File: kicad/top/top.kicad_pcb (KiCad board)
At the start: 2 copper layers, 62 x 119.5 mm, 32 parts, among them J1 OLED_128x64, J2 Conn_01x15, SW1 SW_SPDT, SW2 RotaryEncoder_Switch

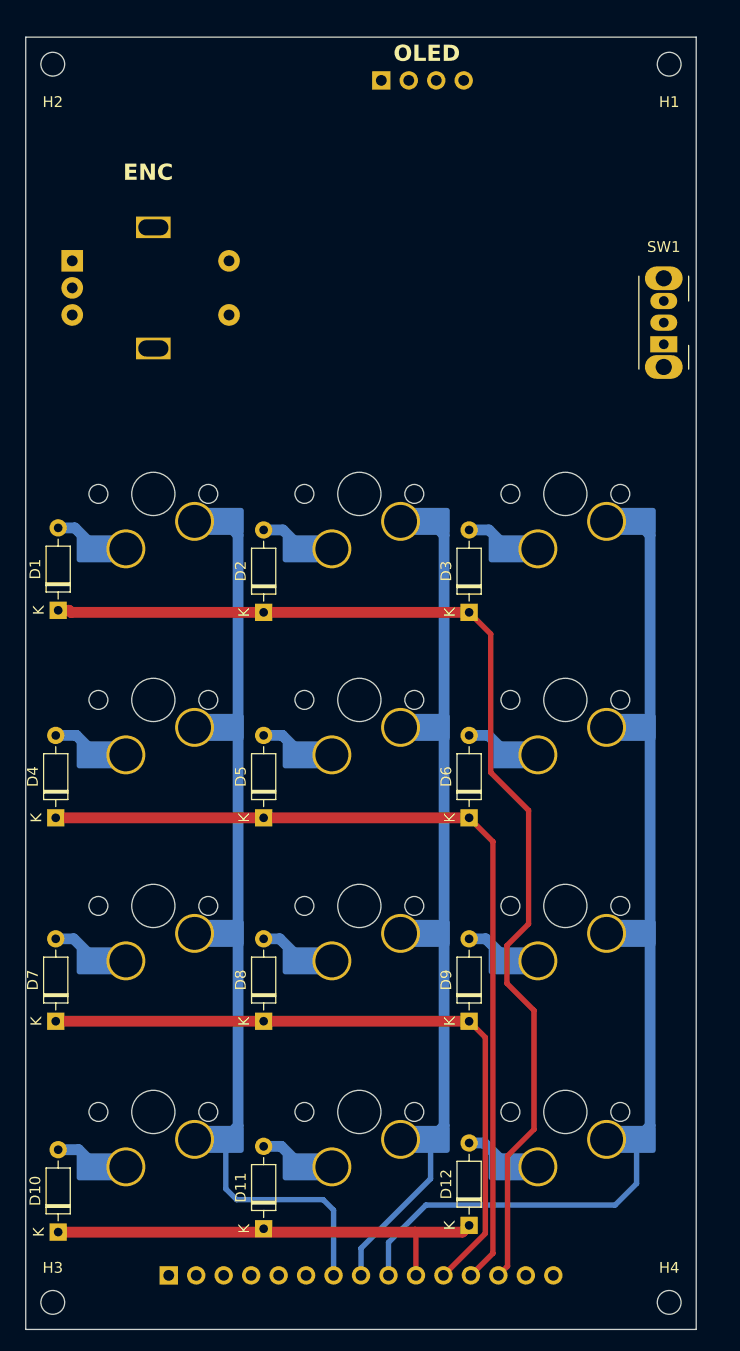
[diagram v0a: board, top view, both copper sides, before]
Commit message: added bottom part of pcb, added 3d model for adafruit feather v2
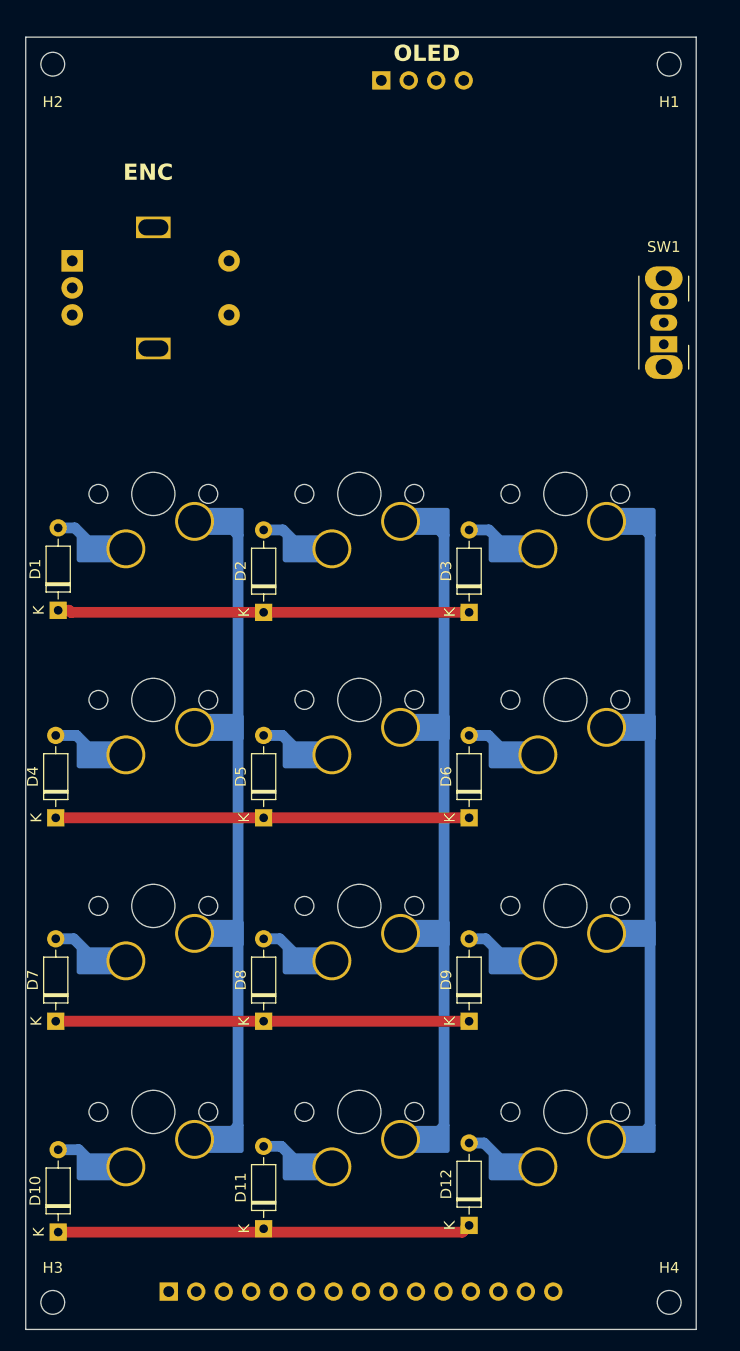
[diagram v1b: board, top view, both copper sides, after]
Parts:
- moved J2 1.50 mm to (27.3, 135.9)
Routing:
- net ROW0: track 104.9 -> 38.1 mm
- net ROW1: track 82.3 -> 38.2 mm
- net COL2: track 90.5 -> 58.2 mm
- net ROW2: track 64.0 -> 38.2 mm
- net COL0: track 79.5 -> 58.2 mm
- net COL1: track 73.4 -> 58.2 mm
- net ROW3: track 42.3 -> 38.3 mm
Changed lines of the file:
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@@
 	(footprint "Connector_PinHeader_2.54mm:PinHeader_1x15_P2.54mm_Vertical"
 		(layer "B.Cu")
-		(at 27.2725 134.425 -90)
+		(at 27.2725 135.925 -90)
 		(descr "Through hole straight pin header, 1x15, 2.54mm pitch, single row")
 		(tags "Through hole pin header THT 1x15 2.54mm single row")
@@
 	)
 	(segment
-		(start 61.0475 120.925)
-		(end 61.0475 109.925)
-		(width 0.5)
-		(layer "F.Cu")
-		(net 1)
-	)
-	(segment
-		(start 58.6025 123.37)
-		(end 61.0475 120.925)
-		(width 0.5)
-		(layer "F.Cu")
-		(net 1)
-	)
-	(segment
-		(start 58.5475 107.425)
-		(end 58.5475 103.925)
-		(width 0.5)
-		(layer "F.Cu")
-		(net 1)
-	)
-	(segment
-		(start 57.0475 87.925)
-		(end 57.0475 75.115)
-		(width 0.5)
-		(layer "F.Cu")
-		(net 1)
-	)
-	(segment
 		(start 18.0475 72.925)
 		(end 18.2375 73.115)
@@
 	)
 	(segment
-		(start 60.5475 91.425)
-		(end 57.0475 87.925)
-		(width 0.5)
-		(layer "F.Cu")
-		(net 1)
-	)
-	(segment
-		(start 60.5475 101.925)
-		(end 60.5475 91.425)
-		(width 0.5)
-		(layer "F.Cu")
-		(net 1)
-	)
-	(segment
 		(start 18.2375 73.115)
 		(end 55.0475 73.115)
@@
 	)
 	(segment
-		(start 57.0475 75.115)
-		(end 55.0475 73.115)
-		(width 0.5)
-		(layer "F.Cu")
-		(net 1)
-	)
-	(segment
-		(start 58.6025 133.575)
-		(end 58.6025 123.37)
-		(width 0.5)
-		(layer "F.Cu")
-		(net 1)
-	)
-	(segment
-		(start 57.7525 134.425)
-		(end 58.6025 133.575)
-		(width 0.5)
-		(layer "F.Cu")
-		(net 1)
-	)
-	(segment
 		(start 17.0475 72.925)
 		(end 18.0475 72.925)
@@
 	)
 	(segment
-		(start 61.0475 109.925)
-		(end 58.5475 107.425)
-		(width 0.5)
-		(layer "F.Cu")
-		(net 1)
-	)
-	(segment
-		(start 58.5475 103.925)
-		(end 60.5475 101.925)
-		(width 0.5)
-		(layer "F.Cu")
-		(net 1)
-	)
-	(segment
 		(start 18.59 65.305)
 		(end 20.5275 67.2425)
@@
 	)
 	(segment
-		(start 55.2125 134.425)
-		(end 57.2475 132.39)
-		(width 0.5)
-		(layer "F.Cu")
-		(net 6)
-	)
-	(segment
 		(start 16.8225 92.115)
 		(end 55.0475 92.115)
@@
 	)
 	(segment
-		(start 57.2475 94.315)
-		(end 55.0475 92.115)
-		(width 0.5)
-		(layer "F.Cu")
-		(net 6)
-	)
-	(segment
-		(start 57.2475 132.39)
-		(end 57.2475 94.315)
-		(width 0.5)
-		(layer "F.Cu")
-		(net 6)
-	)
-	(segment
 		(start 56.83 84.495)
 		(end 58.6275 86.2925)
@@
 	)
 	(segment
-		(start 56.5475 112.425)
-		(end 55.0475 110.925)
-		(width 0.5)
-		(layer "F.Cu")
-		(net 9)
-	)
-	(segment
-		(start 56.5475 130.55)
-		(end 56.5475 112.425)
-		(width 0.5)
-		(layer "F.Cu")
-		(net 9)
-	)
-	(segment
 		(start 16.8225 110.925)
 		(end 55.0475 110.925)
@@
 	)
 	(segment
-		(start 52.6725 134.425)
-		(end 56.5475 130.55)
-		(width 0.5)
-		(layer "F.Cu")
-		(net 9)
-	)
-	(segment
 		(start 55.0475 103.305)
 		(end 56.59 103.305)
@@
 	)
 	(segment
-		(start 50.1325 134.425)
-		(end 50.1325 130.51)
-		(width 0.5)
-		(layer "F.Cu")
-		(net 13)
-	)
-	(segment
-		(start 50.1325 130.51)
-		(end 50.0475 130.425)
-		(width 0.5)
-		(layer "F.Cu")
-		(net 13)
-	)
-	(segment
 		(start 54.4275 130.425)
 		(end 55.0475 129.805)
@@
 	)
 	(segment
-		(start 50.0475 130.425)
-		(end 54.4275 130.425)
-		(width 1)
-		(layer "F.Cu")
-		(net 13)
-	)
-	(segment
 		(start 17.0475 130.425)
-		(end 50.0475 130.425)
+		(end 54.4275 130.425)
 		(width 1)
 		(layer "F.Cu")
@@
 	)
 	(segment
-		(start 41.5475 127.425)
-		(end 33.5475 127.425)
-		(width 0.5)
-		(layer "B.Cu")
-		(net 17)
-	)
-	(segment
-		(start 42.5125 128.39)
-		(end 41.5475 127.425)
-		(width 0.5)
-		(layer "B.Cu")
-		(net 17)
-	)
-	(segment
-		(start 42.5125 134.425)
-		(end 42.5125 128.39)
-		(width 0.5)
-		(layer "B.Cu")
-		(net 17)
-	)
-	(segment
 		(start 33.6825 65.9525)
 		(end 32.4325 64.7025)
@@
 	)
 	(segment
-		(start 32.5475 126.425)
-		(end 32.5475 121.9675)
-		(width 0.5)
-		(layer "B.Cu")
-		(net 17)
-	)
-	(segment
 		(start 32.4325 121.8525)
 		(end 33.6825 120.6025)
@@
 	)
 	(segment
-		(start 33.5475 127.425)
-		(end 32.5475 126.425)
-		(width 0.5)
-		(layer "B.Cu")
-		(net 17)
-	)
-	(segment
-		(start 45.0525 131.92)
-		(end 51.4825 125.49)
-		(width 0.5)
-		(layer "B.Cu")
-		(net 18)
-	)
-	(segment
-		(start 51.4825 125.49)
-		(end 51.4825 121.8525)
-		(width 0.5)
-		(layer "B.Cu")
-		(net 18)
-	)
-	(segment
 		(start 51.4825 64.7025)
 		(end 52.7325 65.9525)
@@
 	)
 	(segment
-		(start 45.0525 134.425)
-		(end 45.0525 131.92)
-		(width 0.5)
-		(layer "B.Cu")
-		(net 18)
-	)
-	(segment
 		(start 52.7325 120.6025)
 		(end 51.4825 121.8525)
@@
 		(layer "B.Cu")
 		(net 19)
-	)
-	(segment
-		(start 70.5325 125.94)
-		(end 70.5325 121.8525)
-		(width 0.5)
-		(layer "B.Cu")
-		(net 19)
-	)
-	(segment
-		(start 51.0475 127.925)
-		(end 68.5475 127.925)
-		(width 0.5)
-		(layer "B.Cu")
-		(net 19)
-	)
-	(segment
-		(start 47.5925 131.38)
-		(end 51.0475 127.925)
-		(width 0.5)
-		(layer "B.Cu")
-		(net 19)
-	)
-	(segment
-		(start 47.5925 134.425)
-		(end 47.5925 131.38)
-		(width 0.5)
-		(layer "B.Cu")
-		(net 19)
-	)
-	(segment
-		(start 68.5475 127.925)
-		(end 70.5325 125.94)
-		(width 0.5)
-		(layer "B.Cu")
-		(net 19)

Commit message: delete duplicate top folder, finished wiring on bottom pcb, need better wiring on top pcb
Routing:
- net +3.3V: track 0.00 -> 154.9 mm
- net OLED_SCL: track 0.00 -> 133.6 mm
- net OLED_SDA: track 0.00 -> 126.0 mm
- net ROW0: track 38.1 -> 105.6 mm
- net ROW1: track 38.2 -> 83.6 mm
- net ROW2: track 38.2 -> 65.2 mm
- net COL2: track 58.2 -> 84.2 mm
- net COL0: track 58.2 -> 76.4 mm
- net COL1: track 58.2 -> 74.9 mm
- net ROW3: track 38.3 -> 43.9 mm
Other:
- board text added: "MODE_SW"

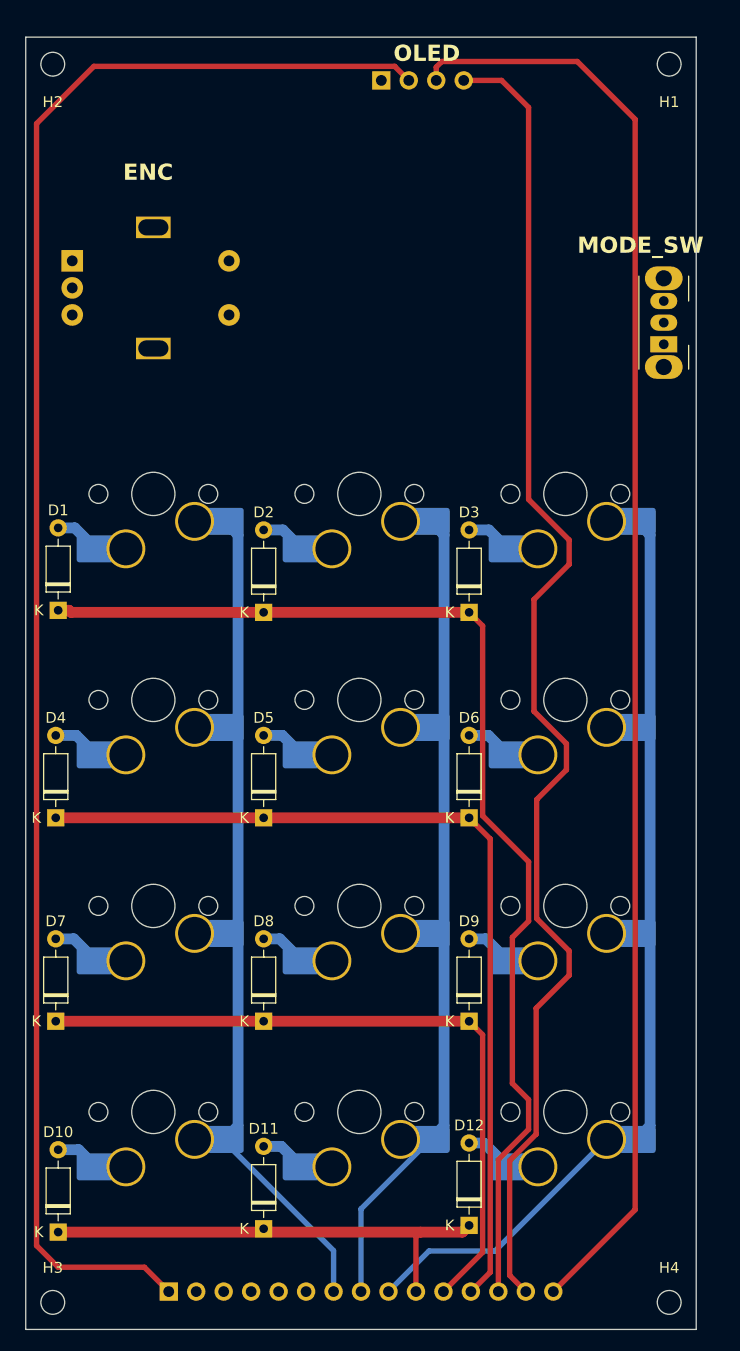
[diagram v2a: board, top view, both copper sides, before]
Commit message: on bottom pcb moved signal connections from back copper to front, left most back copper as ground plane. aligned pins and pin sockets on top and bottom pcb, centered them.
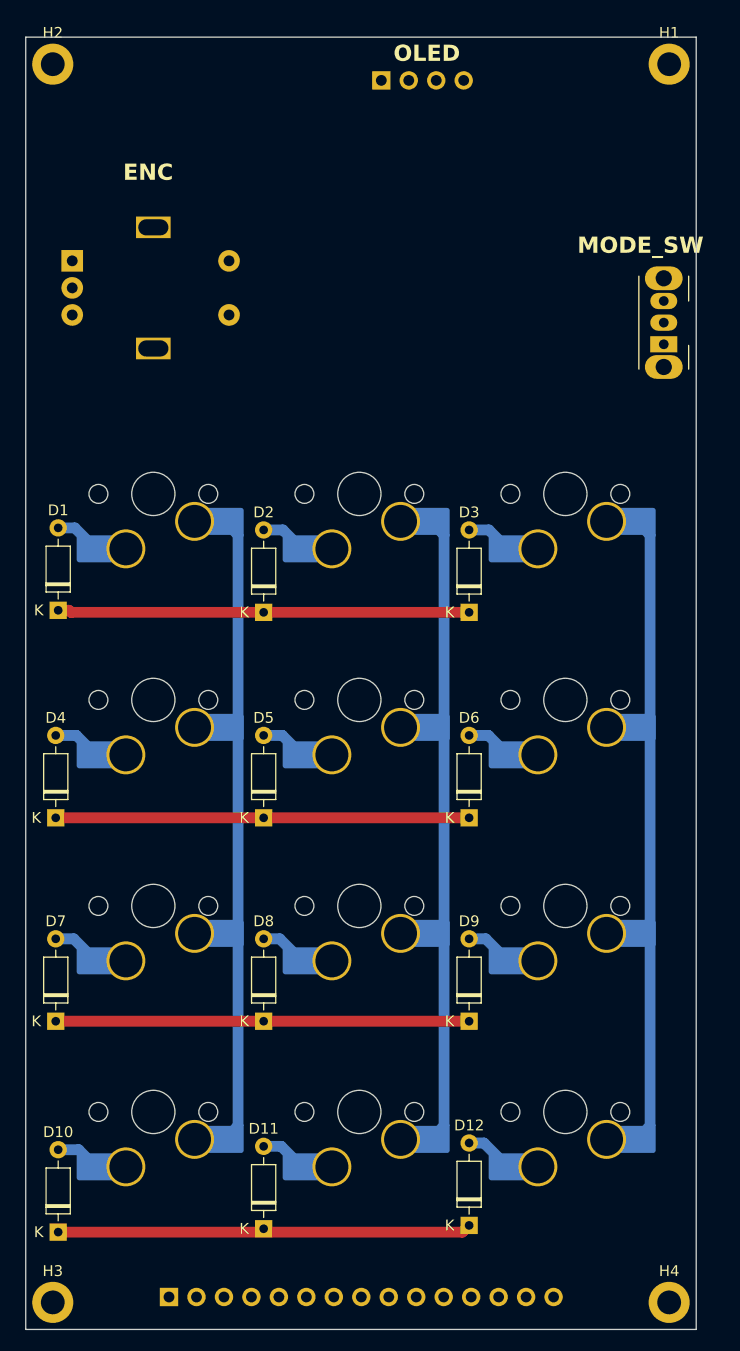
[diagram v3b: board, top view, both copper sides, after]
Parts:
- H1, H2, H3, H4: value MountingHole -> MountingHole_Pad; footprint MountingHole:MountingHole_2.2mm_M2 -> MountingHole:MountingHole_2.2mm_M2_DIN965_Pad
- moved J2 0.50 mm to (27.3, 136.4)
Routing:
- net +3.3V: track 154.9 -> 0.00 mm
- net OLED_SCL: track 133.6 -> 0.00 mm
- net OLED_SDA: track 126.0 -> 0.00 mm
- net ROW0: track 105.6 -> 38.1 mm
- net ROW1: track 83.6 -> 38.2 mm
- net ROW2: track 65.2 -> 38.2 mm
- net COL2: track 84.2 -> 58.2 mm
- net COL0: track 76.4 -> 58.2 mm
- net COL1: track 74.9 -> 58.2 mm
- net ROW3: track 43.9 -> 38.3 mm

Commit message: finished all connections on top pcb, can be improved.
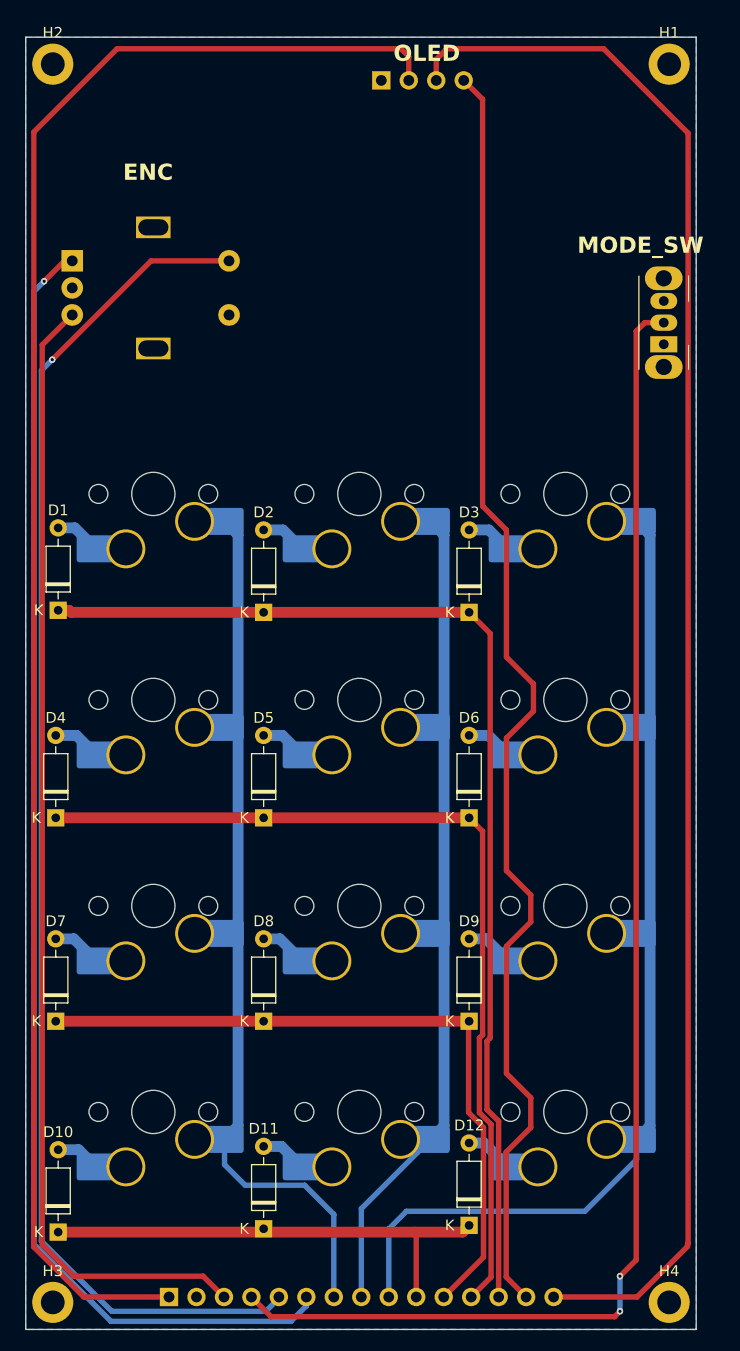
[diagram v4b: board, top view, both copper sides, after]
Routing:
- net +3.3V: track 0.00 -> 157.9 mm
- net OLED_SCL: track 0.00 -> 146.2 mm
- net BT_SELECT: track 0.00 -> 128.8 mm, vias 0 -> 2
- net ENC_SW: track 0.00 -> 127.3 mm, vias 0 -> 1
- net ENC_CLK: track 0.00 -> 122.4 mm, vias 0 -> 1
- net OLED_SDA: track 0.00 -> 120.7 mm
- net ENC_DT: track 0.00 -> 105.9 mm
- net ROW0: track 38.1 -> 102.8 mm
- net ROW1: track 38.2 -> 84.4 mm
- net COL2: track 58.2 -> 91.9 mm
- net ROW2: track 38.2 -> 65.8 mm
- net COL0: track 58.2 -> 80.2 mm
- net COL1: track 58.2 -> 75.4 mm
- net ROW3: track 38.3 -> 44.3 mm
- added copper zone on B.Cu, net GND
